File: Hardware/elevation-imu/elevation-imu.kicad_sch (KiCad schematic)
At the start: 22 parts, among them J1 Conn_02x04_Odd_Even, J2 Conn_01x03_Male, Q1 BSS138, Q2 BSS138, Q3 BSS138, U1 LSM6DSO32, U2 74HCT541, U3 TC2015-3.3VxCTTR

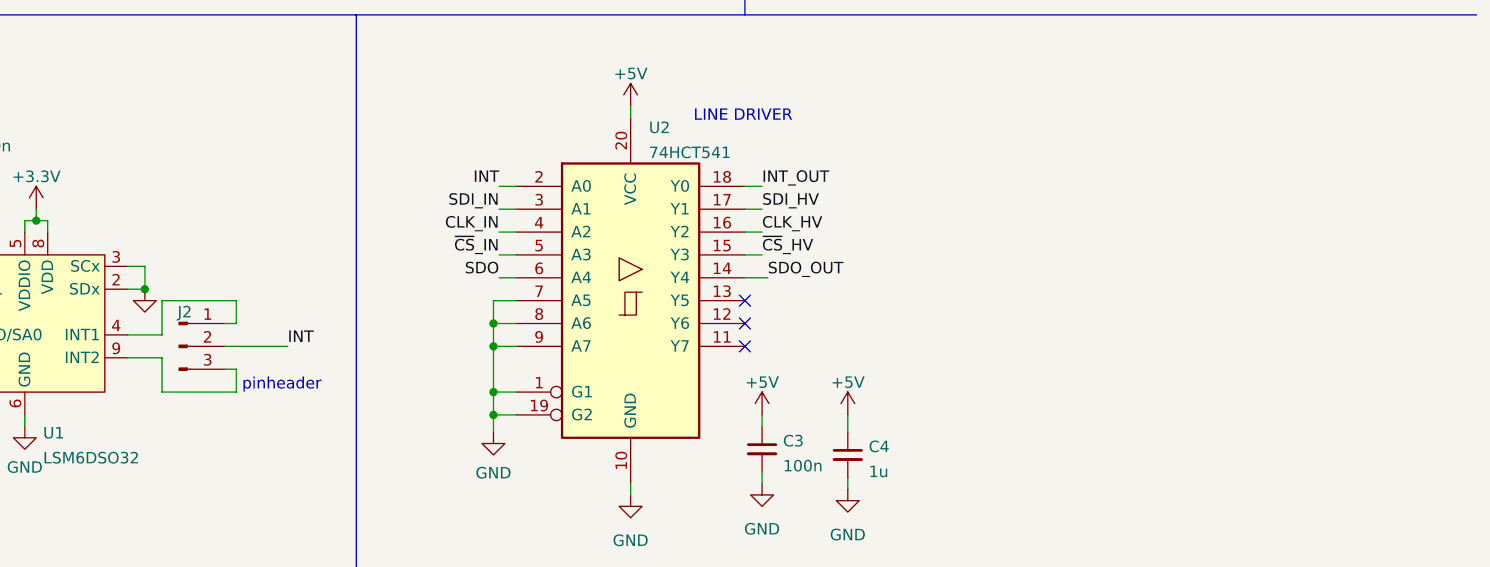
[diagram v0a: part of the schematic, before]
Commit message: E-IMU: Floorplanning and layout
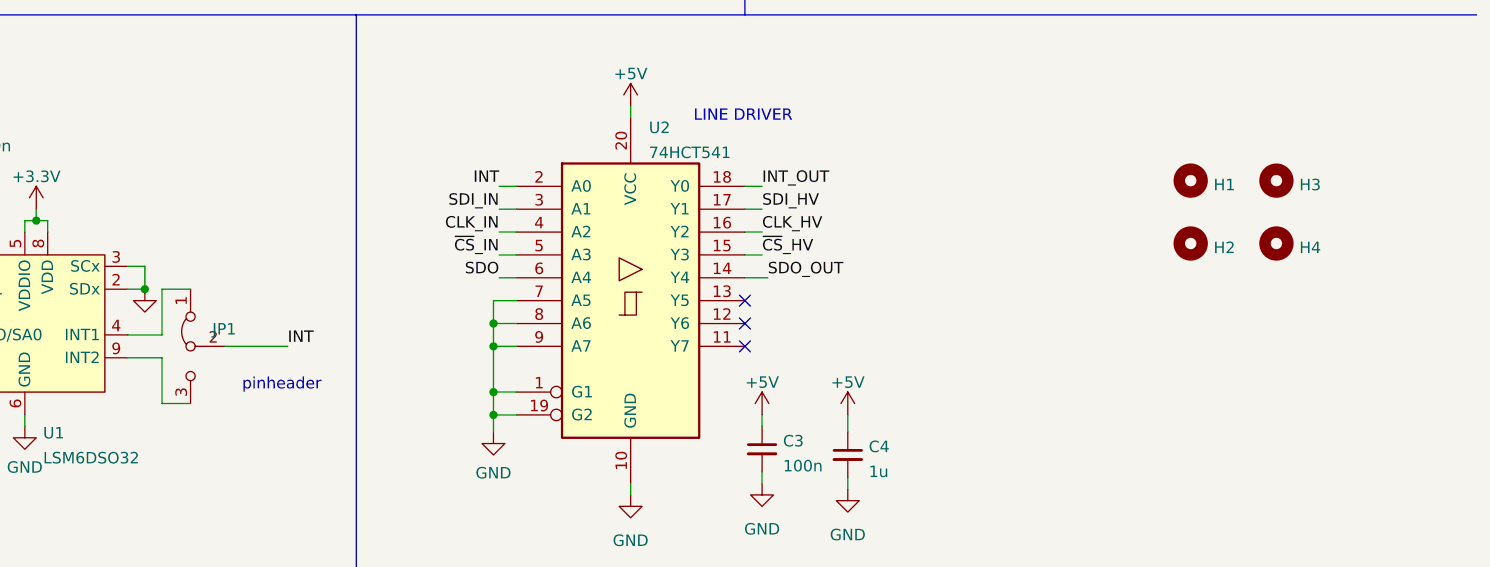
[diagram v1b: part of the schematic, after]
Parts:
- removed J2: Conn_01x03_Male, Connector_PinHeader_2.54mm:PinHeader_1x03_P2.54mm_Horizontal, symbol Connector:Conn_01x03_Male
- added H1, H2, H3, H4: MountingHole, MountingHole:MountingHole_3.2mm_M3, symbol Mechanical:MountingHole
- added JP1: Jumper_3_Bridged12, Jumper:SolderJumper-3_P1.3mm_Bridged12_Pad1.0x1.5mm_NumberLabels, symbol Jumper:Jumper_3_Bridged12
- Q1, Q2, Q3: footprint Package_TO_SOT_SMD:SOT-23 -> Package_TO_SOT_SMD:SOT-323_SC-70
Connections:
- net INT: now also JP1.2 (C)
- net at U1.4 (INT1): now also JP1.1 (A)
- net at U1.9 (INT2): now also JP1.3 (B)

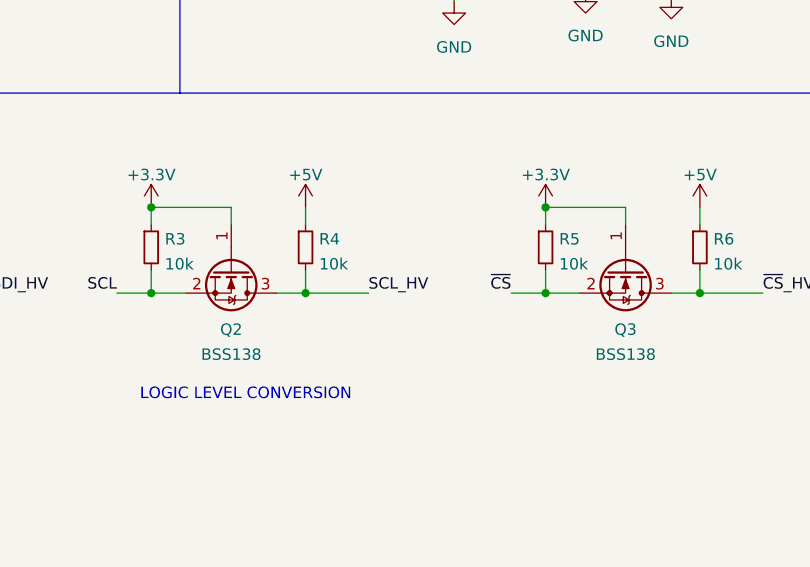
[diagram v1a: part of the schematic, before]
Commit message: EIMU: Fix disconnected SCL
This commit fixes a mistake where SCL and SCK were not connected.
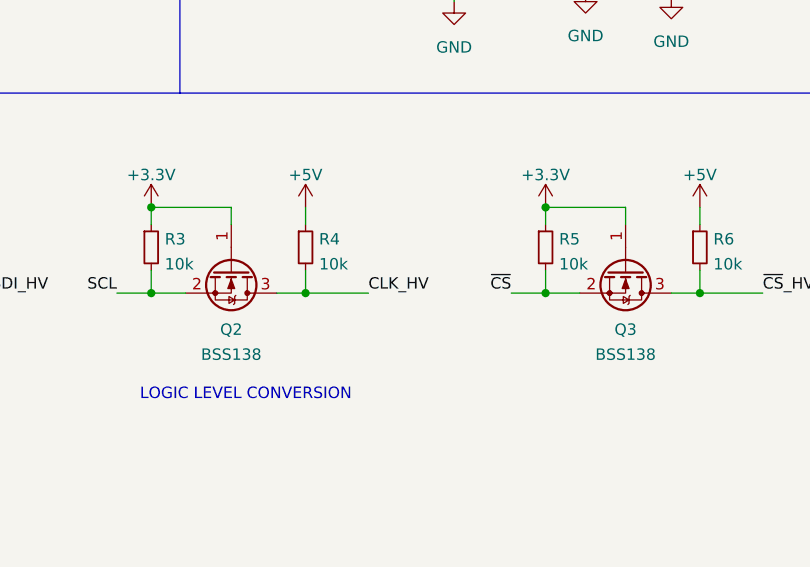
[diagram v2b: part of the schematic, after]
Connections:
- net SCL_HV is gone; now on net CLK_HV: Q2.3 (D), R4.2
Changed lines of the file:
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@@
     (effects (font (size 1.27 1.27)) (justify left bottom))
   )
-  (label "SCL_HV" (at 153.67 142.875 0)
+  (label "CLK_HV" (at 153.67 142.875 0)
     (effects (font (size 1.27 1.27)) (justify left bottom))
   )

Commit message: Add intereferometer radio hardware
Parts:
- added TP1, TP2, TP3, TP4, TP5, TP6, TP7, TP8, TP9: TestPoint, TestPoint:TestPoint_THTPad_D1.0mm_Drill0.5mm, symbol Connector:TestPoint
- J1: footprint Connector_PinHeader_2.54mm:PinHeader_2x04_P2.54mm_Vertical -> MyParts:RJ45-UPDOWN_P100MIL
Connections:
- net CLK_IN: now also J1.6 (Pin_6), TP6.1; no longer J1.4 (Pin_4)
- net GND: now also J1.5 (Pin_5), TP8.1; no longer J1.8 (Pin_8)
- net INT_OUT: now also J1.3 (Pin_3); no longer J1.6 (Pin_6)
- net SCL: now also TP3.1
- net SDI: now also TP1.1
- net SDI_IN: now also TP2.1
- net SDO: now also TP9.1
- net SDO_OUT: now also J1.8 (Pin_8), TP7.1; no longer J1.3 (Pin_3)
- net ~{CS}: now also TP5.1
- net ~{CS}_IN: now also J1.4 (Pin_4), TP4.1; no longer J1.5 (Pin_5)
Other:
- moved on the sheet: Q1, Q2, Q3, R1, R2, R3, R4, R5, R6
